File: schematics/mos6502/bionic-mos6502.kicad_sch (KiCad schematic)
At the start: 6 parts, among them J1 Bionic-P135, J2 Bionic-P245, U1 W65C816S, U3 11AA010-I/TO

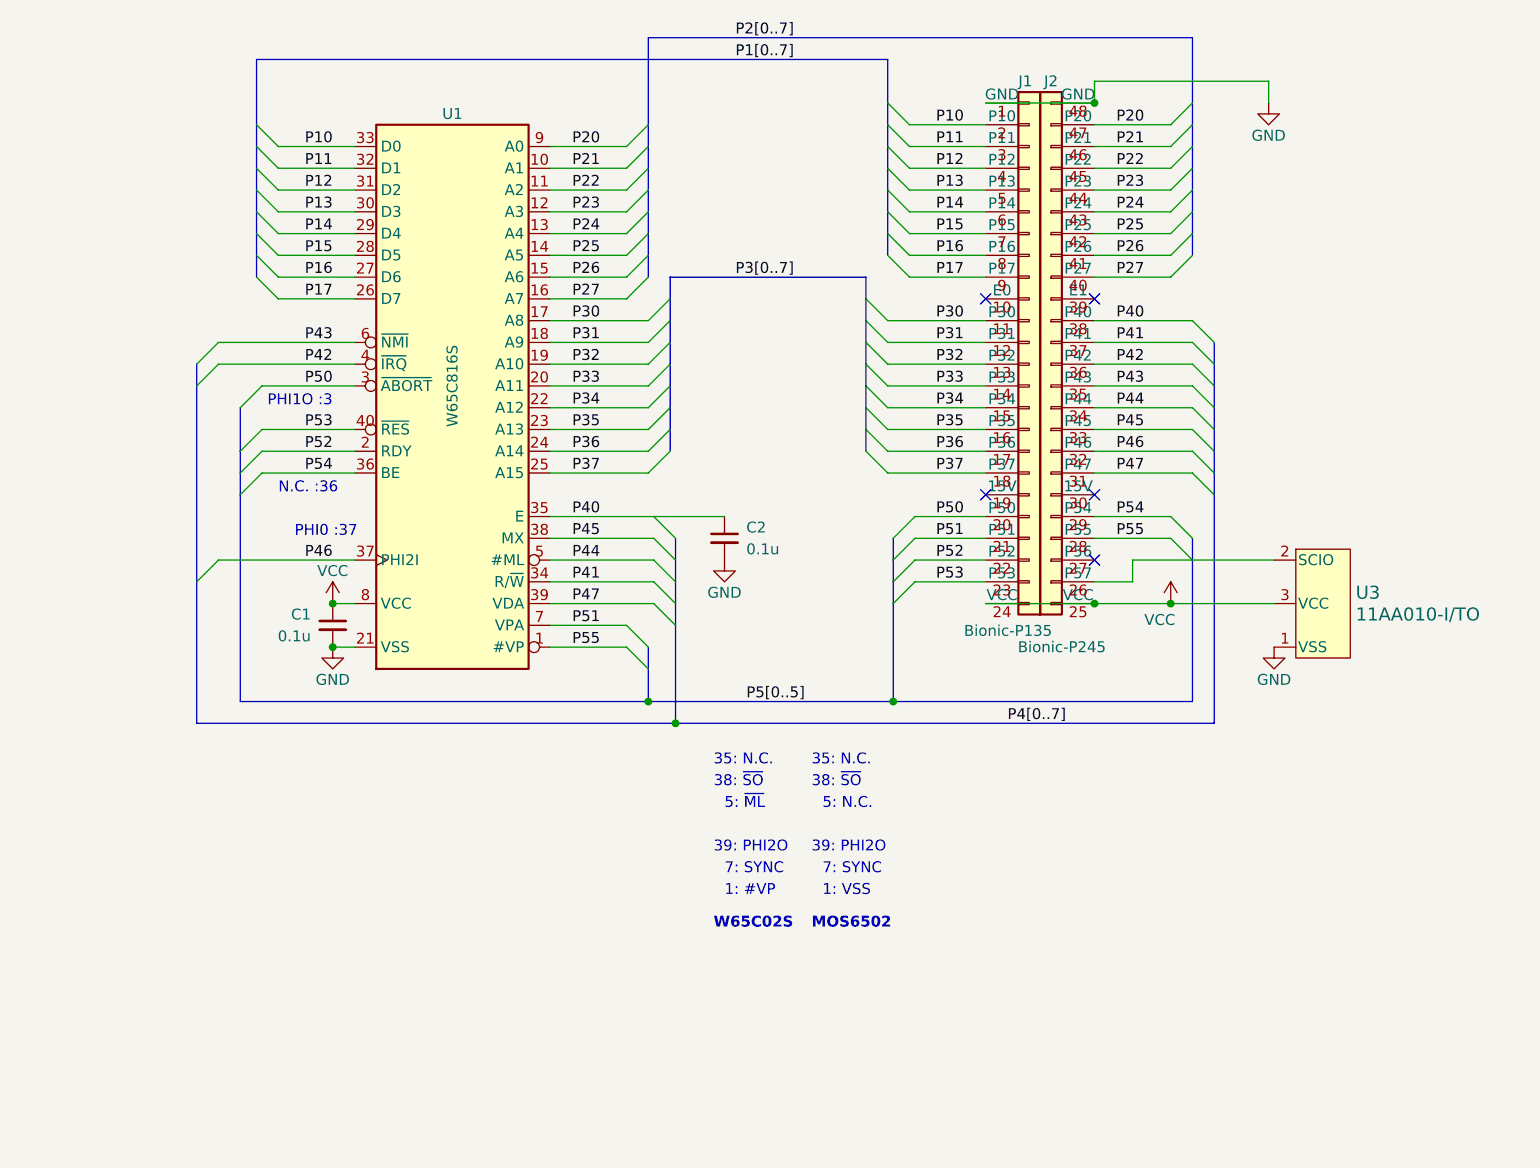
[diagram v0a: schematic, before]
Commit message: [MOS6502] Read control signals as bus
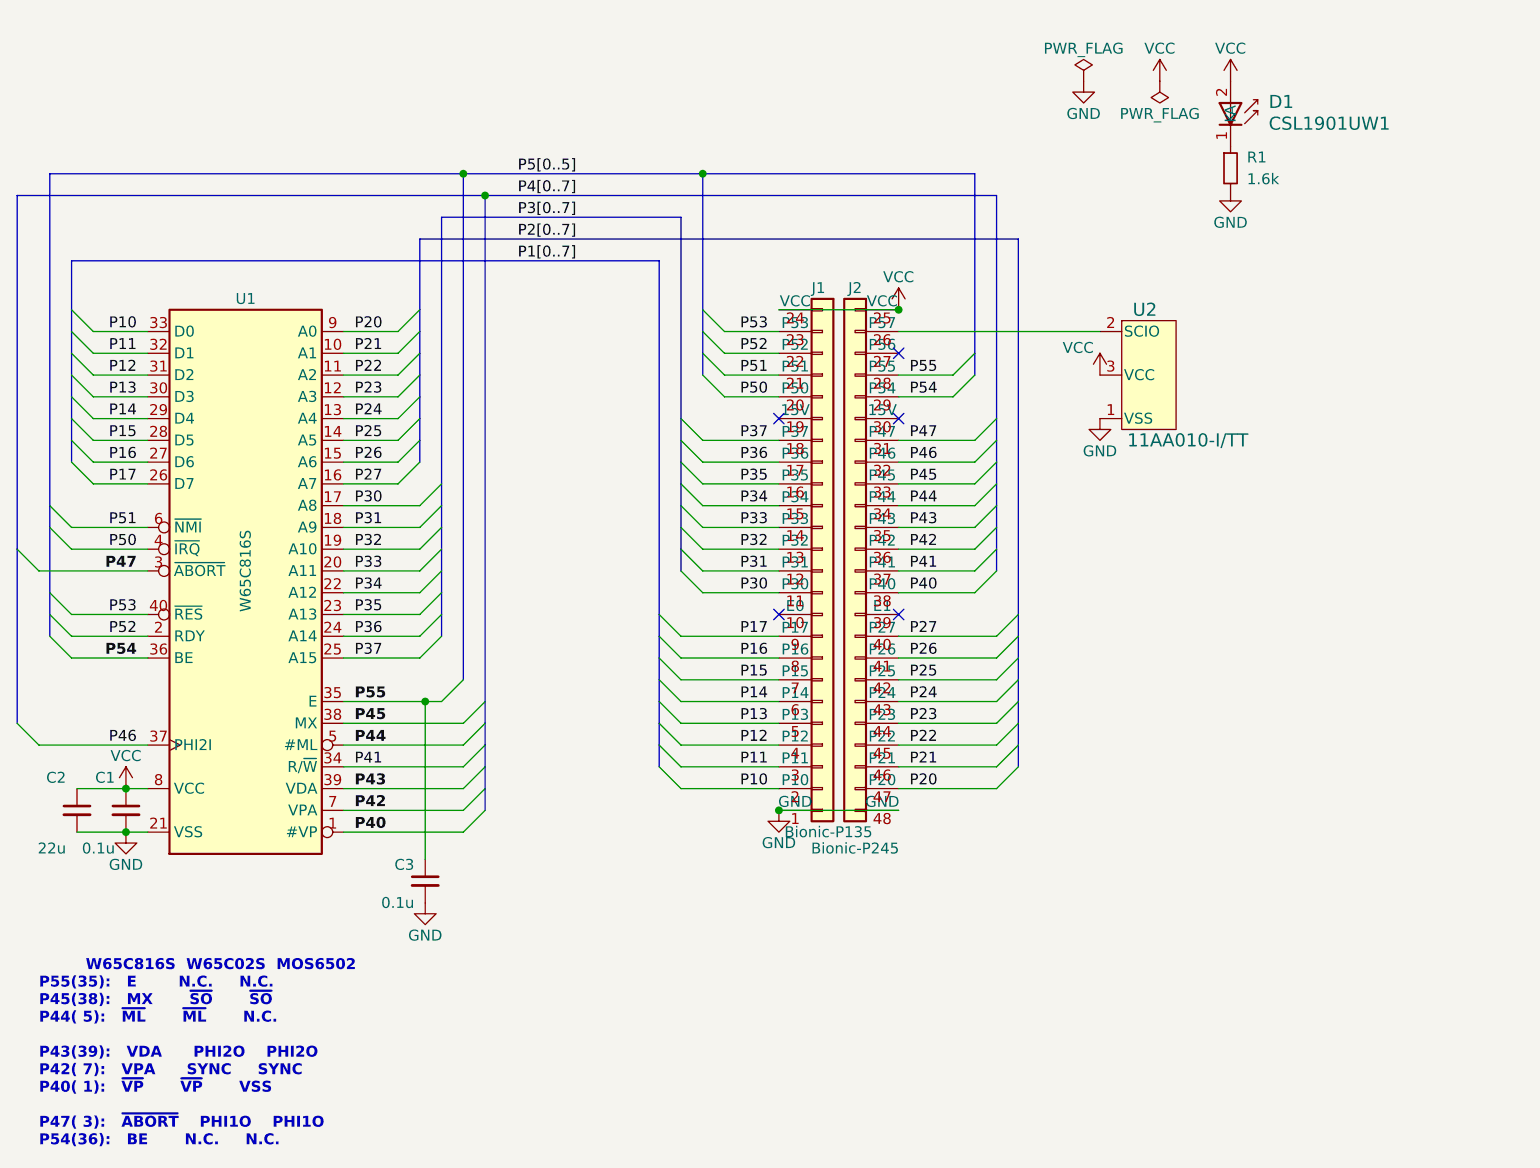
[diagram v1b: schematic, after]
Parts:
- removed U3: 11AA010-I/TO, microchip:TO-92_MC_MCH, symbol 0-LocalLibrary:11AA010-I_TO
- added C3: 0.1u, Capacitor_SMD:C_0603_1608Metric_Pad1.08x0.95mm_HandSolder, symbol Device:C_Small
- added D1: CSL1901UW1, 0-LocalLibrary:LED_CSL1901UW1_ROM, symbol 0-LocalLibrary:CSL1901UW1
- added R1: 1.6k, Resistor_SMD:R_0603_1608Metric_Pad0.98x0.95mm_HandSolder, symbol Device:R_Small
- added U2: 11AA010-I/TT, 0-LocalLibrary:SOT-23_MC_MCH-M, symbol 0-LocalLibrary:11AA010-I_TT
- C1: footprint Capacitor_THT:C_Disc_D3.4mm_W2.1mm_P2.50mm -> Capacitor_SMD:C_0603_1608Metric_Pad1.08x0.95mm_HandSolder
- C2: value 0.1u -> 22u; footprint Capacitor_THT:C_Disc_D3.4mm_W2.1mm_P2.50mm -> Capacitor_SMD:C_0603_1608Metric_Pad1.08x0.95mm_HandSolder
- J1: footprint connector:Bionic-P135_Vertical -> 0-LocalLibrary:Bionic-P135_Vertical
- J2: footprint connector:Bionic-P245_Vertical -> 0-LocalLibrary:Bionic-P245_Vertical
- U1: footprint Package_DIP:DIP-40_W15.24mm -> 0-LocalLibrary:DIP-40_W15.24mm_Socket
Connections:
- net GND: now also C3.2, R1.2, U2.1 (VSS)
- net P40: now also U1.1 (#VP); no longer C2.1, U1.35 (E)
- net P42: now also U1.7 (VPA); no longer U1.4 (~{IRQ})
- net P43: now also U1.39 (VDA); no longer U1.6 (~{NMI})
- net P47: now also U1.3 (~{ABORT}); no longer U1.39 (VDA)
- net P50: now also U1.4 (~{IRQ}); no longer U1.3 (~{ABORT})
- net P51: now also U1.6 (~{NMI}); no longer U1.7 (VPA)
- net P55: now also U1.35 (E), C3.1; no longer U1.1 (#VP)
- net VCC: now also C2.1, D1.2 (A), U2.3 (VCC)
- net at J2.26 (P57): now also U2.2 (SCIO)
- new net: D1.1 (K), R1.1
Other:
- note added: "W65C816S W65C02S MOS6502 P55(35): E N.C. N.C. P45(38): MX ~{SO} ~{SO} P44( 5): ~{ML} ~{ML} N.C. P43(39): VDA PHI2O PHI2O P42( 7): VPA SYNC SYNC P40( 1): ~{VP} ~{VP} VSS P47( 3): ~{ABORT} PHI1O PHI1O P54(36): BE N.C. N.C."
- note removed: "1: #VP"
- note removed: "1: VSS"
- note removed: "35: N.C."
- note removed: "38: ~{SO}"
- note removed: "39: PHI2O"
- note removed: "5: N.C."
- note removed: "5: ~{ML}"
- note removed: "7: SYNC"
- note removed: "MOS6502"
- note removed: "N.C. :36"
- note removed: "PHI0 :37"
- note removed: "PHI1O :3"
- note removed: "W65C02S"
- moved on the sheet: C1, U1

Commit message: [MOS6502] Add W65C816 E signal to control bus
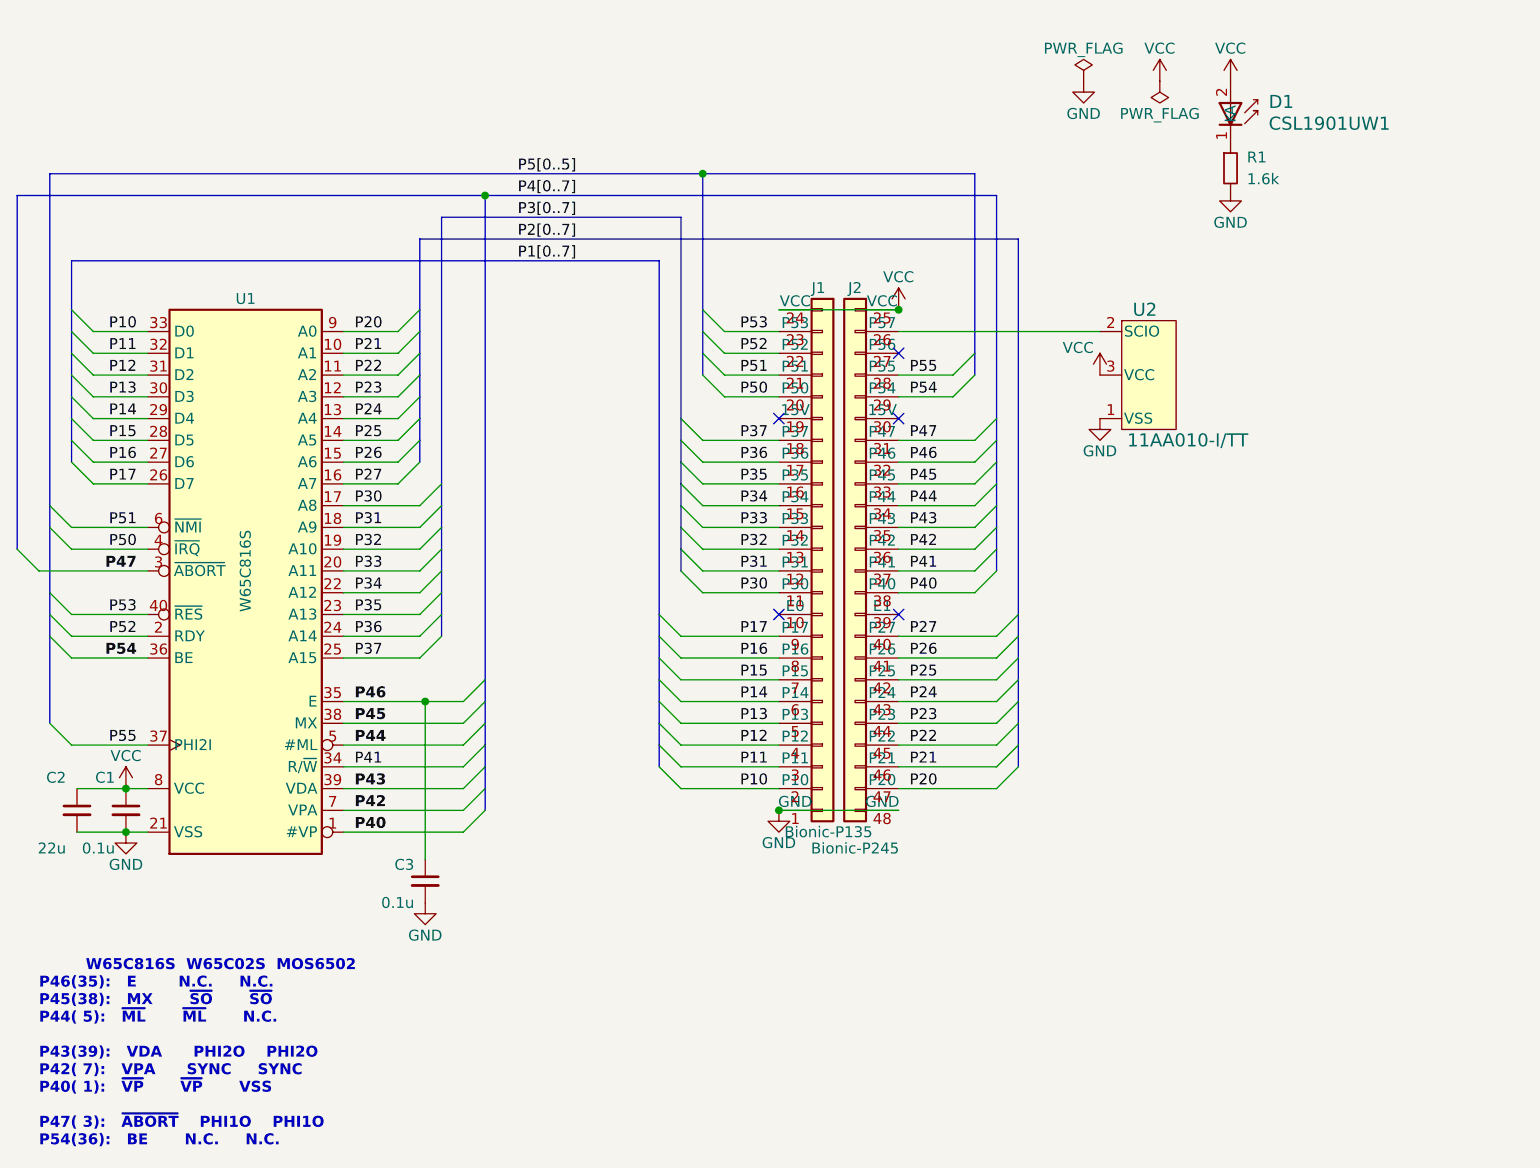
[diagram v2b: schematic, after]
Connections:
- net P46: now also C3.1, U1.35 (E); no longer U1.37 (PHI2I)
- net P55: now also U1.37 (PHI2I); no longer C3.1, U1.35 (E)
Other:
- note added: "W65C816S W65C02S MOS6502 P46(35): E N.C. N.C. P45(38): MX ~{SO} ~{SO} P44( 5): ~{ML} ~{ML} N.C. P43(39): VDA PHI2O PHI2O P42( 7): VPA SYNC SYNC P40( 1): ~{VP} ~{VP} VSS P47( 3): ~{ABORT} PHI1O PHI1O P54(36): BE N.C. N.C."
- note removed: "W65C816S W65C02S MOS6502 P55(35): E N.C. N.C. P45(38): MX ~{SO} ~{SO} P44( 5): ~{ML} ~{ML} N.C. P43(39): VDA PHI2O PHI2O P42( 7): VPA SYNC SYNC P40( 1): ~{VP} ~{VP} VSS P47( 3): ~{ABORT} PHI1O PHI1O P54(36): BE N.C. N.C."
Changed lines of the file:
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@@
   (title_block
     (title "BionicMOS6502")
-    (date "2024-04-29")
-    (rev "6")
+    (date "2024-05-05")
+    (rev "7")
     (company "Tadashi G. Takaoka")
   )
   (junction (at 146.05 128.27) (diameter 0) (color 0 0 0 0)
-  )
-  (junction (at 109.22 53.975) (diameter 0) (color 0 0 0 0)
   )
   (junction (at 69.85 130.81) (diameter 0) (color 0 0 0 0)
@@
     (stroke (width 0) (type default))
   )
-  (bus_entry (at 59.69 120.65) (size -2.54 -2.54)
+  (bus_entry (at 63.5 120.65) (size -2.54 -2.54)
     (stroke (width 0) (type default))
   )
@@
     (stroke (width 0) (type default))
   )
-  (bus_entry (at 106.68 115.57) (size 2.54 -2.54)
+  (bus_entry (at 109.22 115.57) (size 2.54 -2.54)
     (stroke (width 0) (type default))
   )
@@
     (stroke (width 0) (type default))
   )
-  (bus (pts (xy 60.96 53.975) (xy 109.22 53.975))
+  (bus (pts (xy 60.96 53.975) (xy 137.16 53.975))
     (stroke (width 0) (type default))
   )
@@
     (stroke (width 0) (type default))
   )
-  (bus (pts (xy 109.22 53.975) (xy 137.16 53.975))
-    (stroke (width 0) (type default))
-  )
   (wire (pts (xy 95.25 123.19) (xy 109.22 123.19))
     (stroke (width 0) (type default))
@@
     (stroke (width 0) (type default))
   )
-  (bus (pts (xy 57.15 97.79) (xy 57.15 118.11))
-    (stroke (width 0) (type default))
-  )
   (bus (pts (xy 132.08 115.57) (xy 132.08 118.11))
     (stroke (width 0) (type default))
@@
     (stroke (width 0) (type default))
   )
-  (bus (pts (xy 109.22 53.975) (xy 109.22 113.03))
-    (stroke (width 0) (type default))
-  )
   (wire (pts (xy 95.25 102.87) (xy 104.14 102.87))
     (stroke (width 0) (type default))
@@
     (stroke (width 0) (type default))
   )
+  (bus (pts (xy 60.96 107.95) (xy 60.96 118.11))
+    (stroke (width 0) (type default))
+  )
   (bus (pts (xy 132.08 64.135) (xy 132.08 105.41))
     (stroke (width 0) (type default))
@@
     (stroke (width 0) (type default))
   )
-  (wire (pts (xy 59.69 120.65) (xy 72.39 120.65))
+  (wire (pts (xy 63.5 120.65) (xy 72.39 120.65))
     (stroke (width 0) (type default))
   )
@@
     (stroke (width 0) (type default))
   )
-  (bus (pts (xy 111.76 115.57) (xy 111.76 56.515))
+  (bus (pts (xy 111.76 115.57) (xy 111.76 113.03))
     (stroke (width 0) (type default))
   )
@@
     (stroke (width 0) (type default))
   )
-  (wire (pts (xy 104.775 115.57) (xy 106.68 115.57))
+  (wire (pts (xy 104.775 115.57) (xy 109.22 115.57))
     (stroke (width 0) (type default))
   )
@@
     (stroke (width 0) (type default))
   )
+  (bus (pts (xy 111.76 113.03) (xy 111.76 56.515))
+    (stroke (width 0) (type default))
+  )
   (wire (pts (xy 160.02 107.95) (xy 171.45 107.95))
     (stroke (width 0) (type default))
@@
     (stroke (width 0) (type default))
   )
-  (text "         W65C816S  W65C02S  MOS6502\nP55(35):   E        N.C.     N.C. \nP45(38):   MX       ~{SO}       ~{SO}\nP44( 5):   ~{ML}       ~{ML}       N.C.\n\nP43(39):   VDA      PHI2O    PHI2O\nP42( 7):   VPA      SYNC     SYNC\nP40( 1):   ~{VP}       ~{VP}       VSS\n\nP47( 3):   ~{ABORT}    PHI1O    PHI1O\nP54(36):   BE       N.C.     N.C."
+  (text "         W65C816S  W65C02S  MOS6502\nP46(35):   E        N.C.     N.C. \nP45(38):   MX       ~{SO}       ~{SO}\nP44( 5):   ~{ML}       ~{ML}       N.C.\n\nP43(39):   VDA      PHI2O    PHI2O\nP42( 7):   VPA      SYNC     SYNC\nP40( 1):   ~{VP}       ~{VP}       VSS\n\nP47( 3):   ~{ABORT}    PHI1O    PHI1O\nP54(36):   BE       N.C.     N.C."
     (at 59.69 167.64 0)
     (effects (font (face "Noto Mono") (size 1.27 1.27) (thickness 0.254) bold (color 0 0 255 1)) (justify left bottom))
@@
     (effects (font (size 1.27 1.27)) (justify left bottom))
   )
-  (label "P55" (at 96.52 115.57 0) (fields_autoplaced)
+  (label "P46" (at 96.52 115.57 0) (fields_autoplaced)
     (effects (font (size 1.27 1.27) (thickness 0.254) bold (color 0 0 255 1)) (justify left bottom))
   )
-  (label "P46" (at 71.12 120.65 180) (fields_autoplaced)
+  (label "P55" (at 71.12 120.65 180) (fields_autoplaced)
     (effects (font (size 1.27 1.27) (color 0 0 0 1)) (justify right bottom))
   )

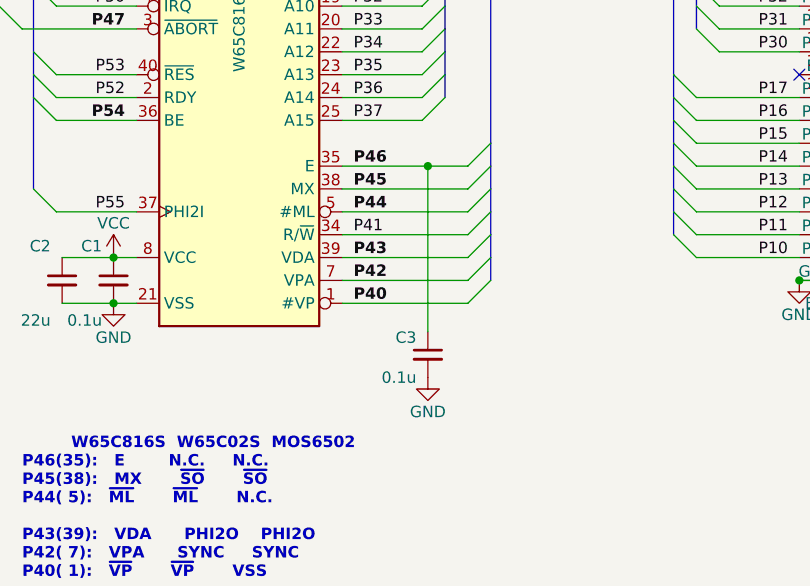
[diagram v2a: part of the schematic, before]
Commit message: [MOS6502] Fix bus conflict with W65C816 bank address
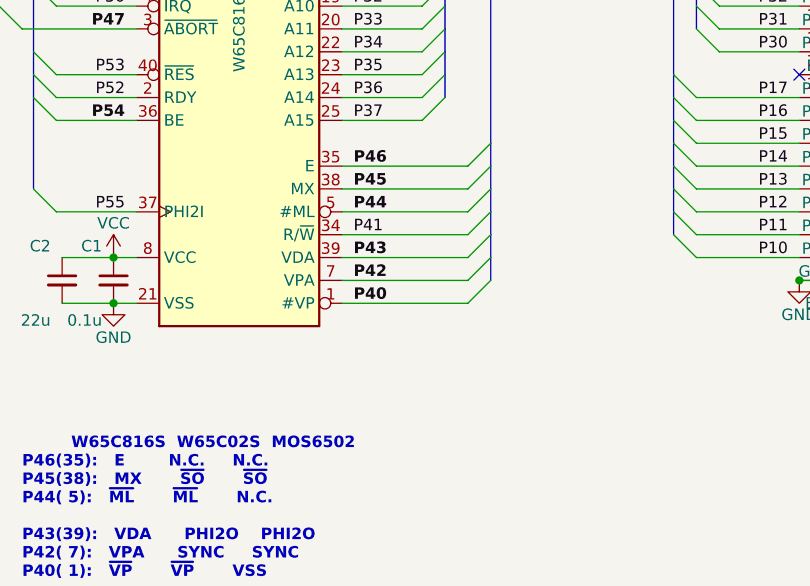
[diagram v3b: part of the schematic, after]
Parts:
- removed C3: 0.1u, Capacitor_SMD:C_0603_1608Metric_Pad1.08x0.95mm_HandSolder, symbol Device:C_Small
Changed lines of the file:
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@@
   (title_block
     (title "BionicMOS6502")
-    (date "2024-05-05")
-    (rev "7")
+    (date "2024-05-10")
+    (rev "8")
     (company "Tadashi G. Takaoka")
   )
@@
   )
   (junction (at 160.02 69.85) (diameter 0) (color 0 0 0 0)
-  )
-  (junction (at 104.775 115.57) (diameter 0) (color 0 0 0 0)
   )
   (junction (at 69.85 125.73) (diameter 0) (color 0 0 0 0)
@@
     (stroke (width 0) (type default))
   )
-  (wire (pts (xy 104.775 115.57) (xy 104.775 133.985))
-    (stroke (width 0) (type default))
-  )
   (wire (pts (xy 69.85 125.73) (xy 72.39 125.73))
     (stroke (width 0) (type default))
@@
     (stroke (width 0) (type default))
   )
-  (wire (pts (xy 104.775 115.57) (xy 109.22 115.57))
+  (wire (pts (xy 95.25 115.57) (xy 109.22 115.57))
     (stroke (width 0) (type default))
   )
@@
   )
   (bus (pts (xy 106.68 59.055) (xy 106.68 90.17))
-    (stroke (width 0) (type default))
-  )
-  (wire (pts (xy 95.25 115.57) (xy 104.775 115.57))
     (stroke (width 0) (type default))
   )
@@
     )
   )
-  (symbol (lib_id "Device:C_Small") (at 104.775 136.525 0) (mirror y) (unit 1)
-    (in_bom yes) (on_board yes) (dnp no)
-    (property "Reference" "C3" (at 103.505 134.62 0)
-      (effects (font (size 1.27 1.27)) (justify left))
-    )
-    (property "Value" "0.1u" (at 103.505 139.065 0)
-      (effects (font (size 1.27 1.27)) (justify left))
-    )
-    (property "Footprint" "Capacitor_SMD:C_0603_1608Metric_Pad1.08x0.95mm_HandSolder" (at 104.775 136.525 0)
-      (effects (font (size 1.27 1.27)) hide)
-    )
-    (property "Datasheet" "~" (at 104.775 136.525 0)
-      (effects (font (size 1.27 1.27)) hide)
-    )
-    (pin "1")
-    (pin "2")
-    (instances
-      (project "bionic-mos6502"
-        (path "/b2640eed-eca1-4dec-a1a1-ceb32e84ee9e"
-          (reference "C3") (unit 1)
-        )
-      )
-    )
-  )
   (symbol (lib_id "power:GND") (at 183.515 82.55 0) (unit 1)
     (in_bom yes) (on_board yes) (dnp no)
@@
         )
       )
-    )
-  )
-  (symbol (lib_id "power:GND") (at 104.775 139.065 0) (unit 1)
-    (in_bom yes) (on_board yes) (dnp no)
-    (property "Reference" "#PWR02" (at 104.775 145.415 0)
-      (effects (font (size 1.27 1.27)) hide)
-    )
-    (property "Value" "GND" (at 104.775 142.875 0)
-      (effects (font (size 1.27 1.27)))
-    )
-    (property "Footprint" "" (at 104.775 139.065 0)
-      (effects (font (size 1.27 1.27)) hide)
-    )
-    (property "Datasheet" "" (at 104.775 139.065 0)
-      (effects (font (size 1.27 1.27)) hide)
-    )
-    (pin "1")
-    (instances
-      (project "bionic-mos6502"
-        (path "/b2640eed-eca1-4dec-a1a1-ceb32e84ee9e"
-          (reference "#PWR02") (unit 1)
-        )
-      )
